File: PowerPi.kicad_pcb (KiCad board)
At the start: 2 copper layers, 65 x 56 mm, 34 parts, among them J1 2444, J3 Conn_01x02, J6 Raspberry_Pi_2_3, J8 2444, Q1 30V 4A 44mΩ, Q2 50nA 150V 200mW 200mA, Q3 30V 4A 44mΩ, U1 XL4015

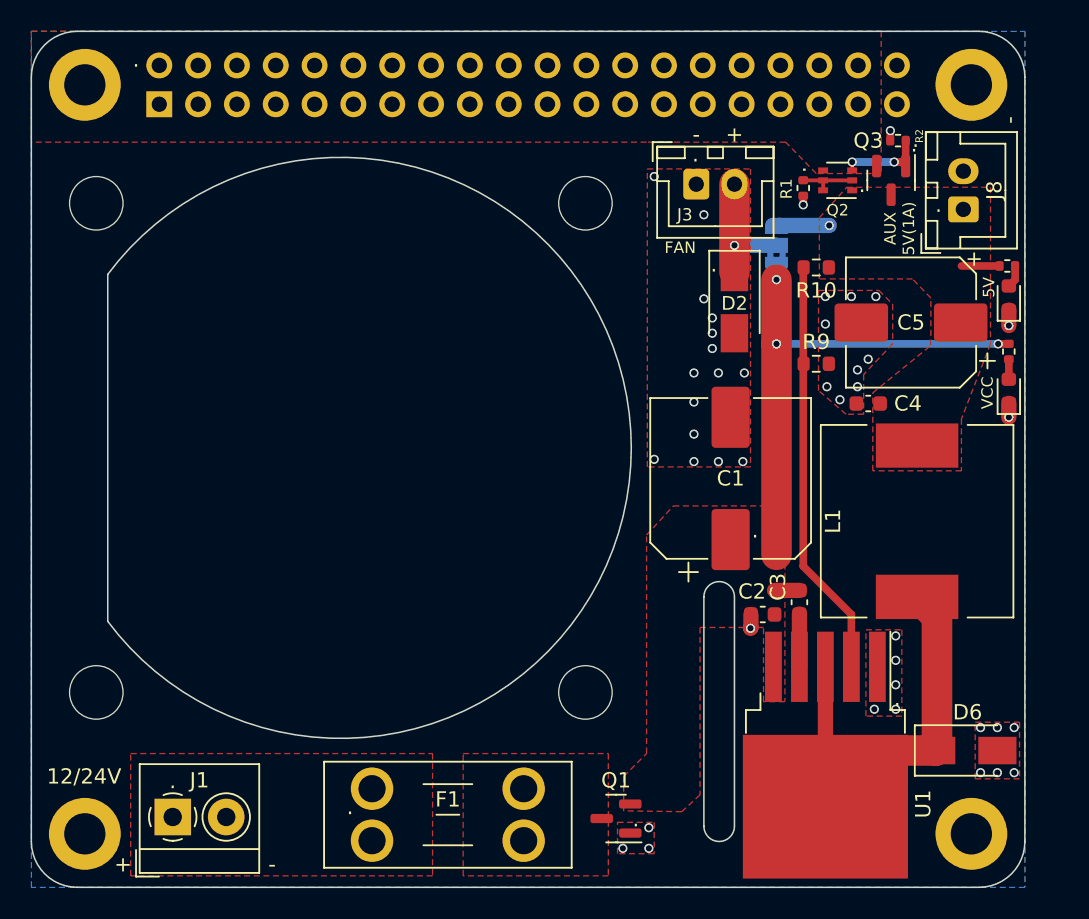
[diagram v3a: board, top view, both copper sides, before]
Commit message: Production Changes
Added LDO Naming to R.silk
Fan JST XH pin +5 and GND swapped to match standard fans
5V pwr LED resistor was 200R now 1KR
24v pwr LED was 1.5k now 10k
Changed sch symbol for XH to not have screws
Added boxes to schematic layout
Added title box entries to schematic
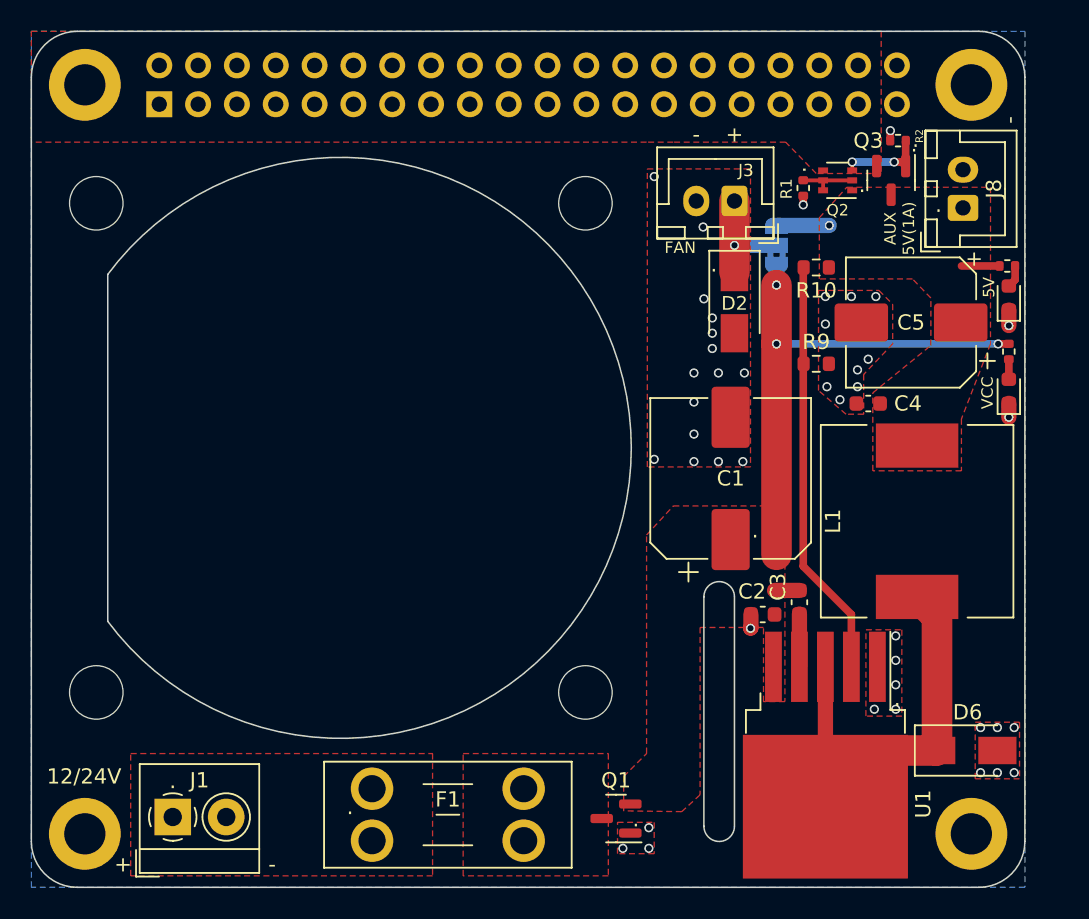
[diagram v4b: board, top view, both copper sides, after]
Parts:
- J3: value Conn_01x02 -> JST XH 01x02
- J8: value 2444 -> JST XH 01x02
- R6: value 200 -> 1kR
- R8: value 1.5K -> 10kR
- moved J3 2.73 mm to (131.2, 64.3), turned to 180 degrees
- moved J8 0.10 mm to (146.2, 64.8)
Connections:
- J3 pad 1: GND -> Net-(D2-Pad1)
- J3 pad 2: Net-(D2-Pad1) -> GND
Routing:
- net Net-(D2-Pad1): track 8.10 -> 7.40 mm
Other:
- board text added: "Designed by Sreenivas Eadara, Produced by LDO Motors"
- board text added: "ElectriPi by Vector 3D"
- board text removed: "Vector 3D PowerPi Designed by Sreenivas Eadara"
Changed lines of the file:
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@@
   (net 29 "unconnected-(J6-Pad38)")
   (net 30 "unconnected-(J6-Pad40)")
-  (net 31 "Net-(Q2-Pad2)")
+  (net 31 "Net-(Q2-Pad6)")
   (net 32 "Net-(Q2-Pad3)")
   (net 33 "Net-(R10-Pad1)")
@@
   (net 44 "unconnected-(J6-Pad24)")
   (footprint "Connector_JST:JST_XH_B2B-XH-A_1x02_P2.50mm_Vertical" (layer "F.Cu")
-    (at 146.225 64.9 90)
+    (at 146.2 64.8 90)
     (descr "JST XH series connector, B2B-XH-A (http://www.jst-mfg.com/product/pdf/eng/eXH.pdf), generated with kicad-footprint-generator")
     (tags "connector JST XH vertical")
@@
     (property "Sheetfile" "PowerPi.kicad_sch")
     (property "Sheetname" "")
-    (property "exclude_from_bom" "")
-    (attr through_hole exclude_from_bom)
+    (attr through_hole)
     (fp_text reference "J8" (at 1.25 2.025 90) (layer "F.SilkS")
       (effects (font (size 1 1) (thickness 0.15)))
     )
-    (fp_text value "2444" (at 1.25 4.6 90) (layer "F.Fab")
+    (fp_text value "JST XH 01x02" (at 1.25 4.6 90) (layer "F.Fab")
       (effects (font (size 1 1) (thickness 0.15)))
     )
@@
       (net 4 "+5V") (pinfunction "E1") (pintype "passive") (zone_connect 1))
     (pad "2" smd rect (at -0.95 0 180) (size 0.65 0.4) (layers "F.Cu" "F.Paste" "F.Mask")
-      (net 31 "Net-(Q2-Pad2)") (pinfunction "B1") (pintype "input"))
+      (net 31 "Net-(Q2-Pad6)") (pinfunction "B1") (pintype "input"))
     (pad "3" smd rect (at -0.95 0.65 180) (size 0.65 0.4) (layers "F.Cu" "F.Paste" "F.Mask")
       (net 32 "Net-(Q2-Pad3)") (pinfunction "C2") (pintype "passive") (zone_connect 2))
@@
       (net 10 "5V_PI") (pinfunction "E2") (pintype "passive") (zone_connect 1))
     (pad "5" smd rect (at 0.95 0 180) (size 0.65 0.4) (layers "F.Cu" "F.Paste" "F.Mask")
-      (net 31 "Net-(Q2-Pad2)") (pinfunction "B2") (pintype "input"))
+      (net 31 "Net-(Q2-Pad6)") (pinfunction "B2") (pintype "input"))
     (pad "6" smd rect (at 0.95 -0.65 180) (size 0.65 0.4) (layers "F.Cu" "F.Paste" "F.Mask")
-      (net 31 "Net-(Q2-Pad2)") (pinfunction "C1") (pintype "passive"))
+      (net 31 "Net-(Q2-Pad6)") (pinfunction "C1") (pintype "passive"))
     (model "${KICAD6_3DMODEL_DIR}/Package_TO_SOT_SMD.3dshapes/SOT-363_SC-70-6.wrl"
       (offset (xyz 0 0 0))
@@
     (fp_line (start 0.525 0.27) (end -0.525 0.27) (layer "F.Fab") (width 0.1))
     (pad "1" smd roundrect (at -0.51 0 270) (size 0.54 0.64) (layers "F.Cu" "F.Paste" "F.Mask") (roundrect_rratio 0.25)
-      (net 31 "Net-(Q2-Pad2)") (pintype "passive"))
+      (net 31 "Net-(Q2-Pad6)") (pintype "passive"))
     (pad "2" smd roundrect (at 0.51 0 270) (size 0.54 0.64) (layers "F.Cu" "F.Paste" "F.Mask") (roundrect_rratio 0.25)
       (net 2 "GND") (pintype "passive"))
@@
       (effects (font (size 1 1) (thickness 0.15)))
     )
-    (fp_text value "200" (at 0 1.17) (layer "F.Fab")
+    (fp_text value "1kR" (at 0 1.17) (layer "F.Fab")
       (effects (font (size 1 1) (thickness 0.15)))
     )
@@
   )
   (footprint "Connector_JST:JST_XH_B2B-XH-A_1x02_P2.50mm_Vertical" (layer "F.Cu")
-    (at 128.75 63.25)
+    (at 131.25 64.35 180)
     (descr "JST XH series connector, B2B-XH-A (http://www.jst-mfg.com/product/pdf/eng/eXH.pdf), generated with kicad-footprint-generator")
     (tags "connector JST XH vertical")
@@
       (effects (font (size 0.8 0.8) (thickness 0.15)))
     )
-    (fp_text value "Conn_01x02" (at 1.25 4.6) (layer "F.Fab")
+    (fp_text value "JST XH 01x02" (at 1.25 4.6) (layer "F.Fab")
       (effects (font (size 1 1) (thickness 0.15)))
     )
@@
     (fp_line (start 0 -1.35) (end 0.625 -2.35) (layer "F.Fab") (width 0.1))
     (fp_line (start -2.45 3.4) (end 4.95 3.4) (layer "F.Fab") (width 0.1))
-    (pad "1" thru_hole roundrect (at 0 0) (size 1.7 2) (drill 1) (layers *.Cu *.Mask) (roundrect_rratio 0.1470588235)
-      (net 2 "GND") (pinfunction "Pin_1") (pintype "passive"))
-    (pad "2" thru_hole oval (at 2.5 0) (size 1.7 2) (drill 1) (layers *.Cu *.Mask)
-      (net 34 "Net-(D2-Pad1)") (pinfunction "Pin_2") (pintype "passive"))
+    (pad "1" thru_hole roundrect (at 0 0 180) (size 1.7 2) (drill 1) (layers *.Cu *.Mask) (roundrect_rratio 0.1470588235)
+      (net 34 "Net-(D2-Pad1)") (pinfunction "Pin_1") (pintype "passive"))
+    (pad "2" thru_hole oval (at 2.5 0 180) (size 1.7 2) (drill 1) (layers *.Cu *.Mask)
+      (net 2 "GND") (pinfunction "Pin_2") (pintype "passive"))
     (model "${KICAD6_3DMODEL_DIR}/Connector_JST.3dshapes/JST_XH_B2B-XH-A_1x02_P2.50mm_Vertical.wrl"
       (offset (xyz 0 0 0))
@@
       (effects (font (size 1 1) (thickness 0.15)))
     )
-    (fp_text value "1.5K" (at 0 1.17 90) (layer "F.Fab")
+    (fp_text value "10kR" (at 0 1.17 90) (layer "F.Fab")
       (effects (font (size 1 1) (thickness 0.15)))
     )
@@
     (property "exclude_from_bom" "")
     (attr exclude_from_pos_files exclude_from_bom)
-    (fp_text reference "JP1" (at 0 1.8 90) (layer "B.SilkS")
+    (fp_text reference "JP1" (at 0 1.95 90) (layer "B.SilkS")
       (effects (font (size 1 1) (thickness 0.15)) (justify mirror))
     )
@@
   (gr_line (start 150.25 56.25) (end 150.25 106.25) (layer "Edge.Cuts") (width 0.1))
   (gr_arc (start 90.25 69.15) (mid 124.500062 80.5) (end 90.25 91.85) (layer "Edge.Cuts") (width 0.1))
-  (gr_text "Vector 3D PowerPi Designed by Sreenivas Eadara" (at 86.4 81.3 270) (layer "B.SilkS")
+  (gr_text "ElectriPi by Vector 3D" (at 88.6 81.1 270) (layer "B.SilkS")
+    (effects (font (size 1.4 1.4) (thickness 0.2)) (justify mirror))
+  )
+  (gr_text "Designed by Sreenivas Eadara, Produced by LDO Motors" (at 86.7 81.8 270) (layer "B.SilkS")
     (effects (font (size 1 1) (thickness 0.15)) (justify mirror))
   )
-  (gr_text "+" (at 131.25 60.9) (layer "B.SilkS")
+  (gr_text "+" (at 131.25 61.9) (layer "B.SilkS")
     (effects (font (size 2 2) (thickness 0.15)) (justify mirror))
   )
-  (gr_text "5V" (at 131.75 65.45 90) (layer "B.SilkS")
+  (gr_text "5V" (at 134.15 64.05 90) (layer "B.SilkS")
     (effects (font (size 1 1) (thickness 0.15)) (justify mirror))
   )
@@
     (effects (font (size 2 2) (thickness 0.15)) (justify mirror))
   )
-  (gr_text "JLCJLCJLC" (at 88.7 80 270) (layer "B.SilkS")
+  (gr_text "JLCJLCJLC" (at 148.95 88 270) (layer "B.SilkS")
     (effects (font (size 1 1) (thickness 0.15)) (justify mirror))
   )
-  (gr_text "-" (at 148.9 61.5 90) (layer "B.SilkS")
+  (gr_text "-" (at 148.7 62.2 90) (layer "B.SilkS")
     (effects (font (size 2 2) (thickness 0.15)) (justify mirror))
   )
@@
     (effects (font (size 2 2) (thickness 0.15)) (justify mirror))
   )
-  (gr_text "VCC" (at 131.75 68.5 90) (layer "B.SilkS")
+  (gr_text "VCC" (at 131.75 69.4 90) (layer "B.SilkS")
     (effects (font (size 1 1) (thickness 0.15)) (justify mirror))
   )
-  (gr_text "+" (at 148.9 65 90) (layer "B.SilkS")
+  (gr_text "+" (at 148.6 64.8 90) (layer "B.SilkS")
     (effects (font (size 2 2) (thickness 0.15)) (justify mirror))
   )
-  (gr_text "-" (at 128.75 60.9) (layer "B.SilkS")
+  (gr_text "-" (at 128.75 61.9) (layer "B.SilkS")
     (effects (font (size 2 2) (thickness 0.15)) (justify mirror))
   )
@@
     (effects (font (size 1 1) (thickness 0.15)))
   )
-  (gr_text "." (at 92.1 55.1) (layer "F.SilkS")
-    (effects (font (size 1 1) (thickness 0.15)))
-  )
   (gr_text "5V" (at 147.9 70 90) (layer "F.SilkS")
     (effects (font (size 0.75 0.75) (thickness 0.15)))
@@
   )
   (gr_text "." (at 136.2 62.3 270) (layer "F.SilkS")
-    (effects (font (size 1 1) (thickness 0.15)))
-  )
-  (gr_text "." (at 128.7 61.3) (layer "F.SilkS")
     (effects (font (size 1 1) (thickness 0.15)))
   )
@@
   )
   (segment (start 148.5 73.7) (end 149.19 73.7) (width 0.5) (layer "F.Cu") (net 1))
+  (segment (start 134 73.7) (end 134 69.85) (width 2) (layer "F.Cu") (net 1))
   (segment (start 135.5 89.825) (end 133.875 89.825) (width 1) (layer "F.Cu") (net 1))
   (segment (start 149.19 73.7) (end 149.2 73.69) (width 0.5) (layer "F.Cu") (net 1))
   (segment (start 134 73.7) (end 134 87.5) (width 2) (layer "F.Cu") (net 1))
-  (segment (start 134 69.5) (end 134 73.7) (width 2) (layer "F.Cu") (net 1))
   (via (at 134 73.7) (size 0.6) (drill 0.4) (layers "F.Cu" "B.Cu") (net 1))
-  (via (at 134 69.5) (size 0.6) (drill 0.4) (layers "F.Cu" "B.Cu") (net 1))
+  (via (at 134 69.85) (size 0.6) (drill 0.4) (layers "F.Cu" "B.Cu") (net 1))
   (via (at 148.5 73.7) (size 0.6) (drill 0.4) (layers "F.Cu" "B.Cu") (net 1))
   (segment (start 134 73.7) (end 148.5 73.7) (width 0.5) (layer "B.Cu") (net 1))
-  (segment (start 134 69.5) (end 134 68.55) (width 1) (layer "B.Cu") (net 1))
+  (segment (start 134 69.85) (end 134 68.55) (width 1) (layer "B.Cu") (net 1))
   (segment (start 149.2 78.5) (end 149.2 77.5875) (width 1) (layer "F.Cu") (net 2))
   (segment (start 132.325 91.4) (end 132.325 92.275) (width 1) (layer "F.Cu") (net 2))
@@
   (via (at 147.35 101.75) (size 0.6) (drill 0.4) (layers "F.Cu" "B.Cu") (free) (net 2))
   (via (at 126 81.25) (size 0.6) (drill 0.4) (layers "F.Cu" "B.Cu") (free) (net 2))
-  (via (at 129.25 65.25) (size 0.6) (drill 0.4) (layers "F.Cu" "B.Cu") (free) (net 2))
+  (via (at 129.2 66.05) (size 0.6) (drill 0.4) (layers "F.Cu" "B.Cu") (free) (net 2))
   (via (at 128.6 81.4) (size 0.6) (drill 0.4) (layers "F.Cu" "B.Cu") (free) (net 2))
   (via (at 129.25 70.75) (size 0.6) (drill 0.4) (layers "F.Cu" "B.Cu") (free) (net 2))
@@
   (segment (start 138.9 91.4) (end 135.75 88.25) (width 0.5) (layer "F.Cu") (net 33))
   (segment (start 135.75 68.725) (end 135.775 68.7) (width 0.5) (layer "F.Cu") (net 33))
-  (segment (start 131.25 67.05) (end 131.25 69) (width 2) (layer "F.Cu") (net 34))
-  (segment (start 131.25 66.65) (end 131.25 63.25) (width 2) (layer "F.Cu") (net 34))
+  (segment (start 131.25 64.35) (end 131.25 69) (width 2) (layer "F.Cu") (net 34))
   (via (at 131.25 67.25) (size 0.6) (drill 0.4) (layers "F.Cu" "B.Cu") (net 34))
   (segment (start 131.25 67.25) (end 134 67.25) (width 1) (layer "B.Cu") (net 34))

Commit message: V1.0 Release
Silkscreen adjustments
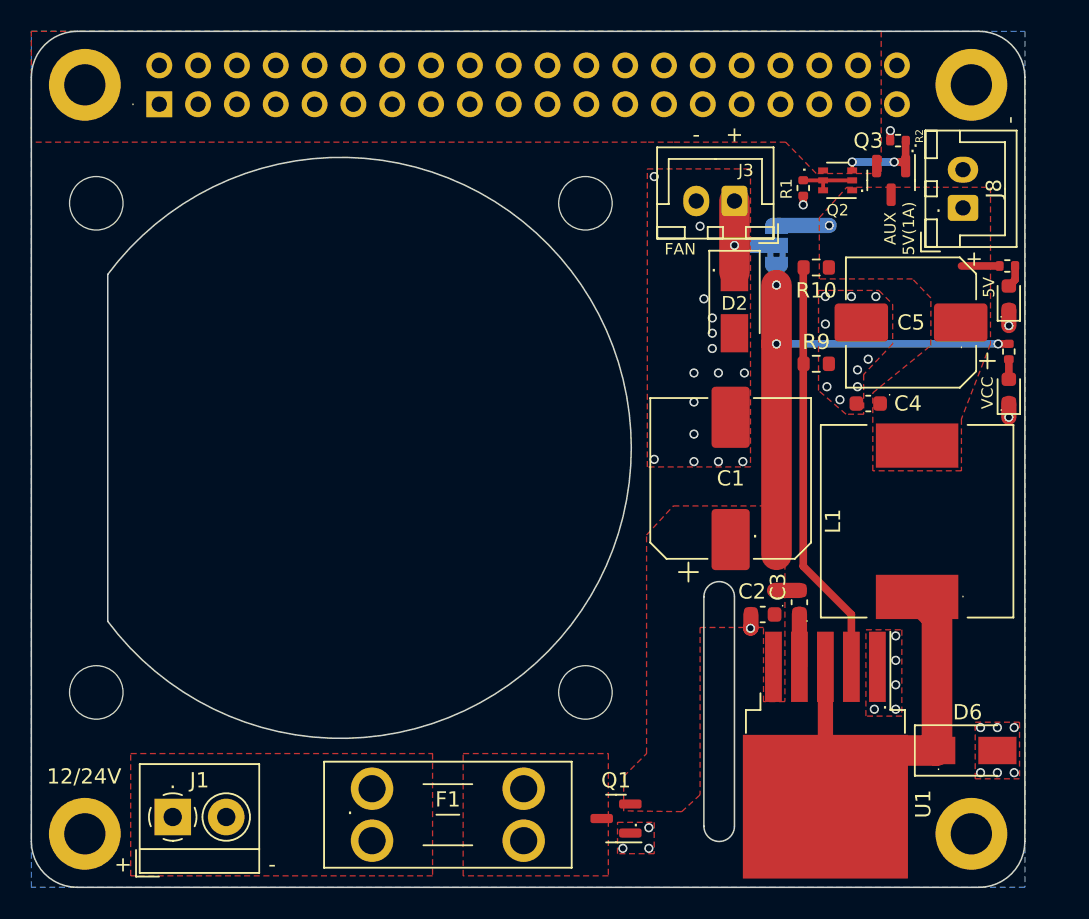
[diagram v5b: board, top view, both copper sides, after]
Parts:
- added G***: LOGO, Logos:LDO Motors Logo, B.Cu at (137.0, 80.8)
- added G***: LOGO, Logos:V3D Logo, B.Cu at (143.7, 85.0)
- added G***: LOGO, Logos:5reen_merge_small, B.Cu at (137.1, 94.5)
